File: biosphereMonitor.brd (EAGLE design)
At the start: 85 x 85 mm, 64 parts, among them IC1 XMEGA32A4AU, IC2 LM35, IC3 FT232RL, IC4 NE555D, IC5 SST25VF040, Q1 16Mhz, Q2 32kHz

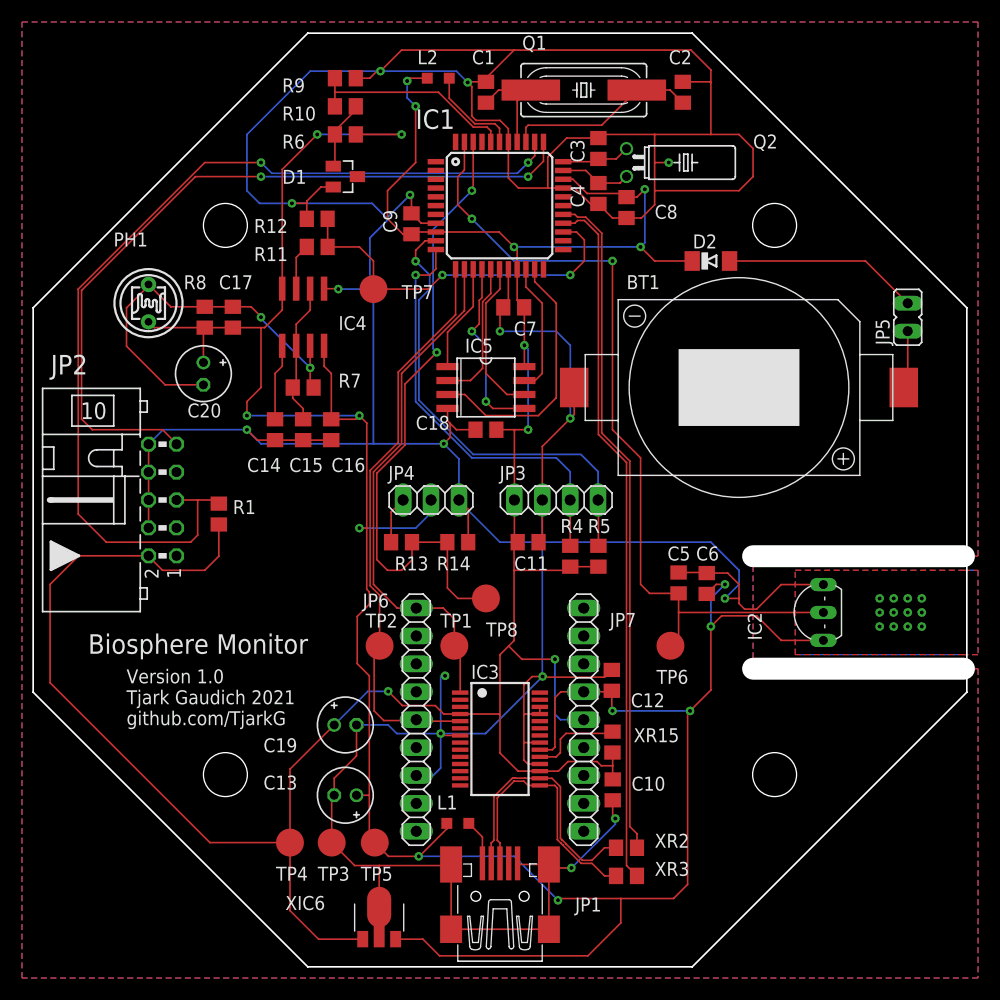
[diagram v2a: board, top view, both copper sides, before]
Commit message: changed some footprints
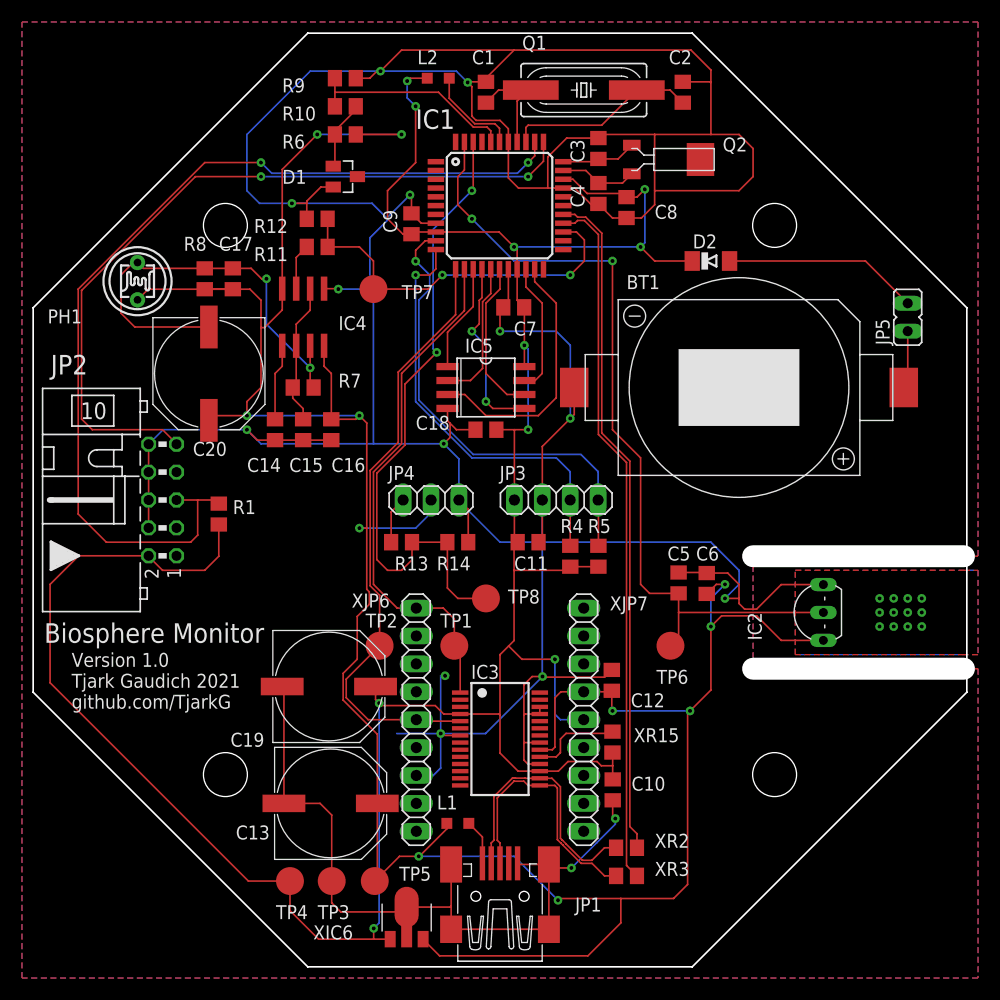
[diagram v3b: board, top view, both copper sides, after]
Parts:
- C13, C19, C20: value 4,7µF -> 220µ; device rcl:E2-5 -> rcl:PANASONIC_G
- Q1: device crystal:HC49UP -> crystal:SM49
- Q2: device crystal:TC38H -> Tjarks_Bauteile (1):MS1V
- moved C19 3.81 mm to (-15.6, -17.0)
- moved C17 3.50 mm to (-24.3, 20.1)
- moved R8 3.50 mm to (-26.9, 20.1)
- moved TP3 3.50 mm to (-15.3, -34.7)
- moved TP4 3.50 mm to (-19.1, -34.7)
- moved TP5 3.50 mm to (-11.4, -34.7)
- moved XIC6 2.50 mm to (-8.50, -38.0)
- moved PH1 2.24 mm to (-33.0, 19.9)
- moved C13 1.53 mm to (-15.4, -27.6), turned to 0 degrees
- moved Q2 0.56 mm to (12.0, 31.0), turned to 180 degrees
- moved C20 0.50 mm to (-26.5, 11.5)
- renumbered JP6 to XJP6, JP7 to XJP7
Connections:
- net N$5: now also Q2.Q1; no longer Q2.1
- net N$6: now also Q2.Q2; no longer Q2.2
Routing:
- net +5V: track 246.8 -> 256.5 mm
- net +3V3: track 246.5 -> 252.1 mm, vias 9 -> 10
- net USB_RX: track 52.3 -> 55.9 mm
- net N$21: track 36.8 -> 40.0 mm
- net GND: track 475.1 -> 477.4 mm, vias 16 -> 15
- net N$5: track 6.25 -> 6.86 mm
- net N$6: track 6.48 -> 7.07 mm

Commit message: optimized layout optics
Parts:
- moved R6 0.23 mm to (-14.0, 33.5)
- moved R10 0.18 mm to (-14.0, 36.0), turned to 180 degrees
- moved R9 0.13 mm to (-14.0, 38.5), turned to 0 degrees
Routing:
- net GND: track 477.4 -> 479.9 mm, vias 15 -> 27
- net 1V: track 19.2 -> 16.7 mm
- net 2.5V: track 6.30 -> 5.71 mm
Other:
- outline, holes or cut-outs redrawn

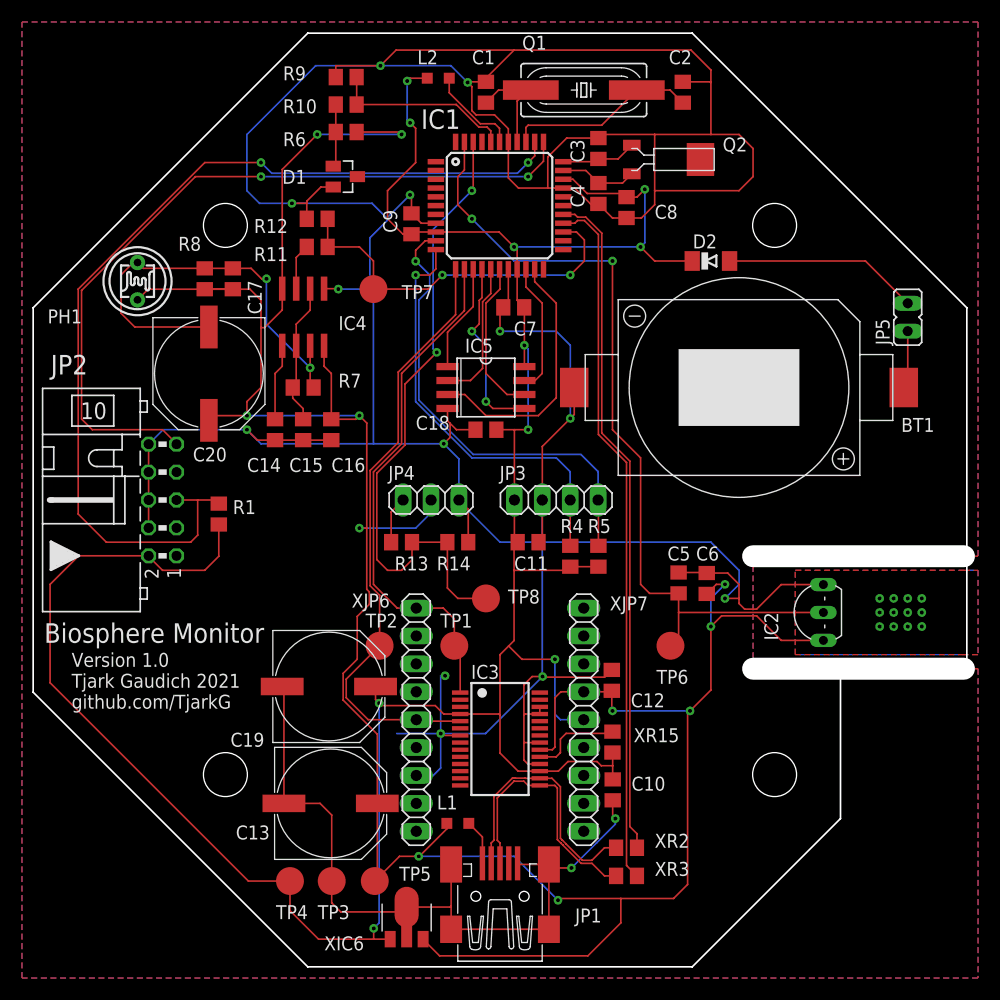
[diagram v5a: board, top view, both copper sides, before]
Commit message: removed unnecesary parts
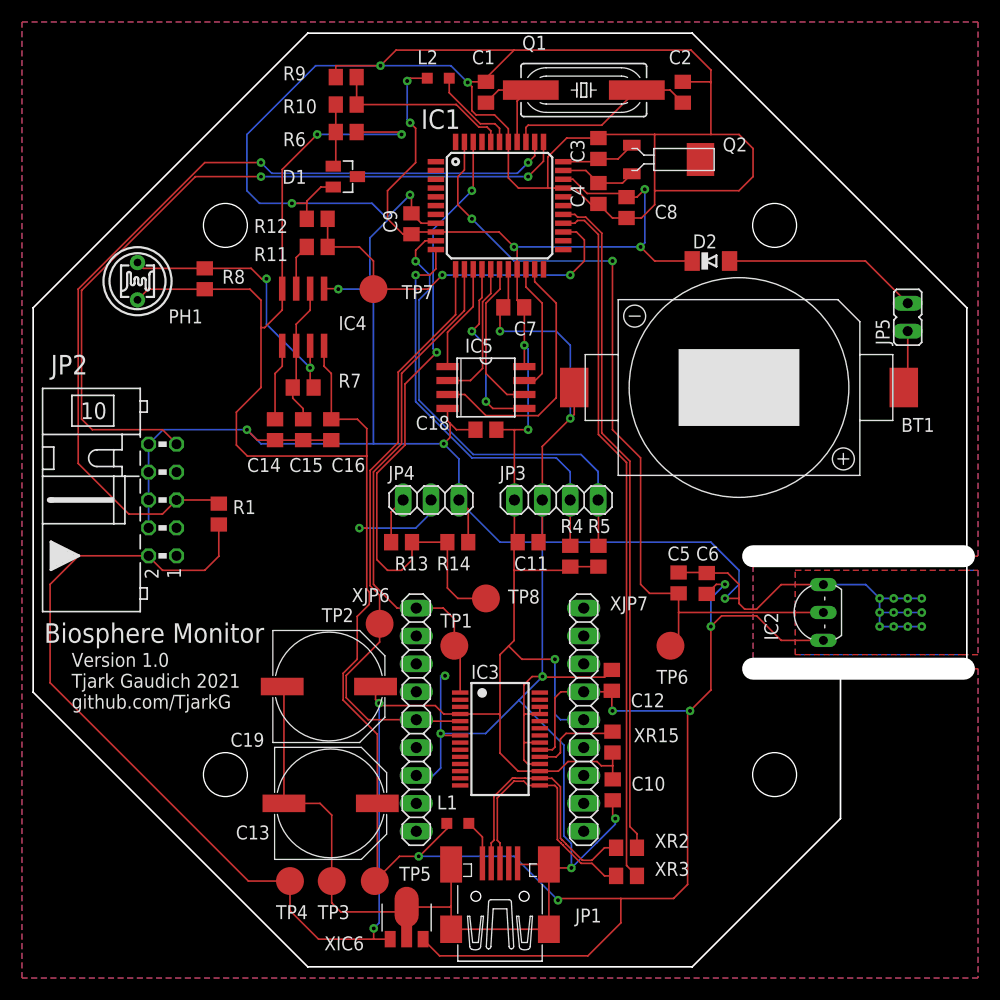
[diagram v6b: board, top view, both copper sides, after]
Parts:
- removed C17: 100n, rcl:C0805
- removed C20: 220µ, rcl:PANASONIC_G
- moved TP2 2.00 mm to (-11.0, -11.3)
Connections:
- net +5V: no longer C17.1, C20.+
- net N$21: no longer C17.2, C20.-
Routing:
- net GND: track 479.9 -> 512.9 mm
- net N$21: track 40.0 -> 26.0 mm
- net N$1: track 88.5 -> 79.9 mm
- net +5V: track 256.5 -> 254.5 mm, vias 11 -> 9

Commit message: moved components away from screws
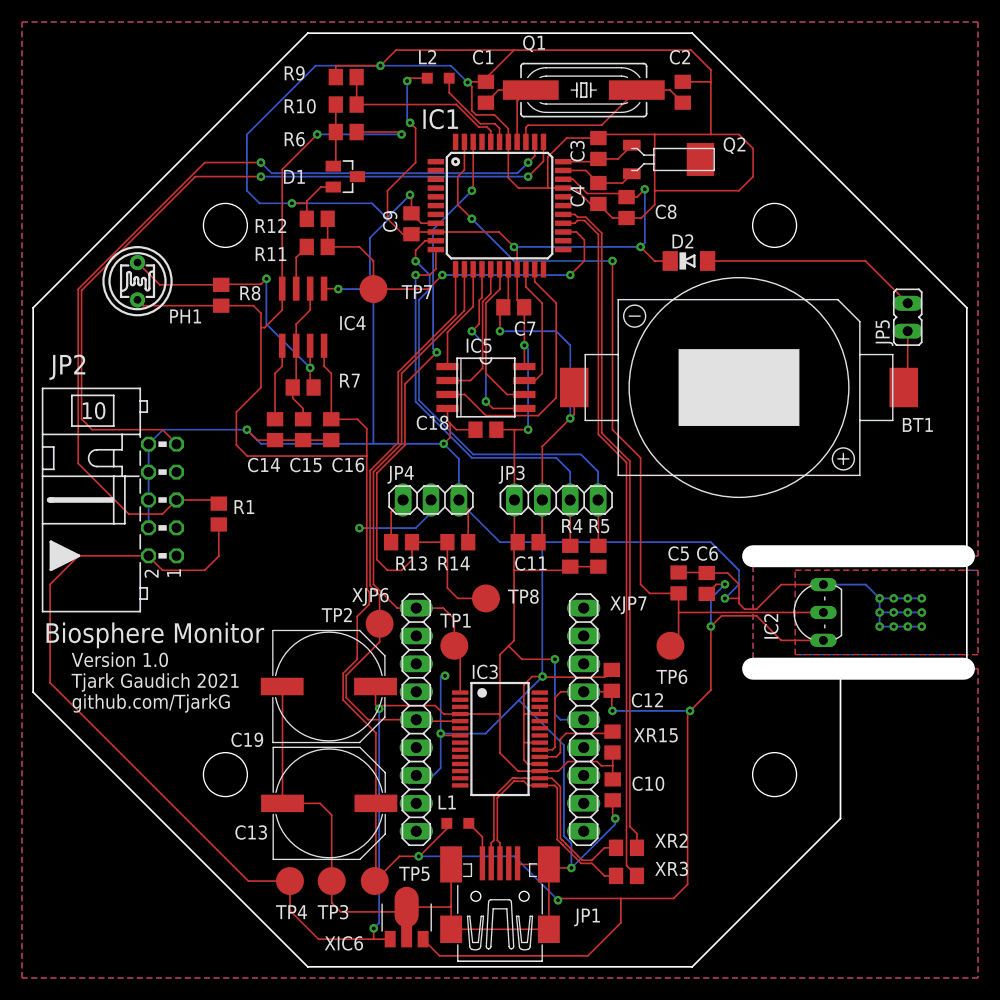
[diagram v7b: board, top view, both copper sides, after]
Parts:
- moved R8 2.12 mm to (-25.4, 18.6)
- moved D2 2.00 mm to (17.2, 21.8)
- moved C13 0.13 mm to (-15.5, -27.6)
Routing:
- net +5V: track 254.5 -> 252.2 mm
- net N$27: track 17.8 -> 19.8 mm
- net +3V3: track 252.1 -> 250.1 mm
- net USB_RX: track 55.9 -> 55.1 mm

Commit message: improved selftest
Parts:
- XIC6: value 78L05F -> 78L33
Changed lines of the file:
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@@
 <attribute name="SPICEPREFIX" value="C" x="-15.58" y="-16.98" size="1.778" layer="27" display="off"/>
 </element>
-<element name="XIC6" library="linear" library_urn="urn:adsk.eagle:library:262" package="SOT89" package3d_urn="urn:adsk.eagle:package:16478/2" value="78L05F" x="-8.5" y="-38" smashed="yes">
+<element name="XIC6" library="linear" library_urn="urn:adsk.eagle:library:262" package="SOT89" package3d_urn="urn:adsk.eagle:package:16478/2" value="78L33" x="-8.5" y="-38" smashed="yes">
 <attribute name="NAME" x="-16" y="-41" size="1.27" layer="25"/>
 <attribute name="POPULARITY" value="5" x="-8.5" y="-38" size="1.778" layer="27" display="off"/>
